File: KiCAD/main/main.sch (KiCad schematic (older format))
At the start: 2 parts

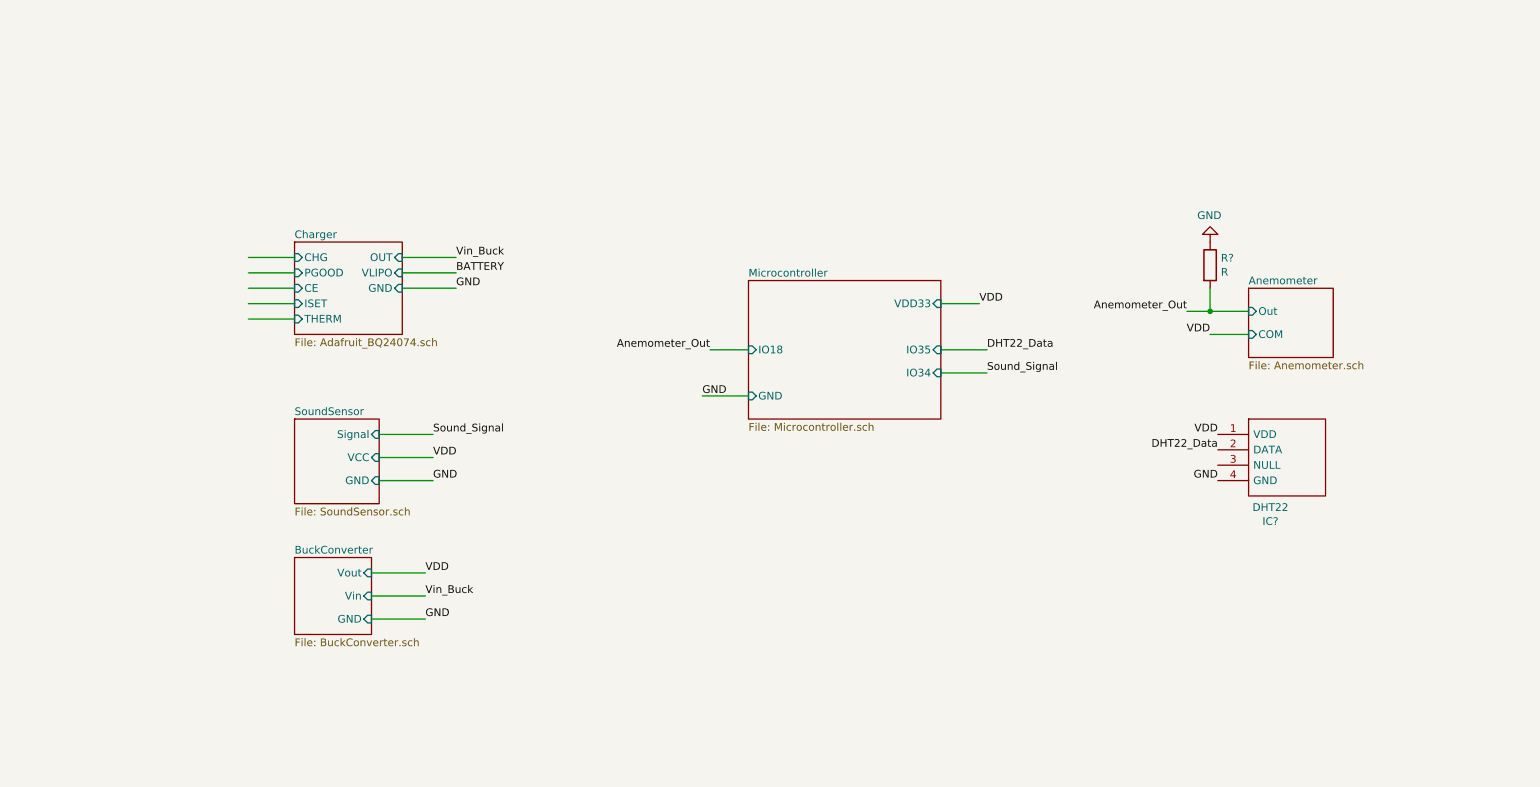
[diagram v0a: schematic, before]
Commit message: Improve readability on main schematic
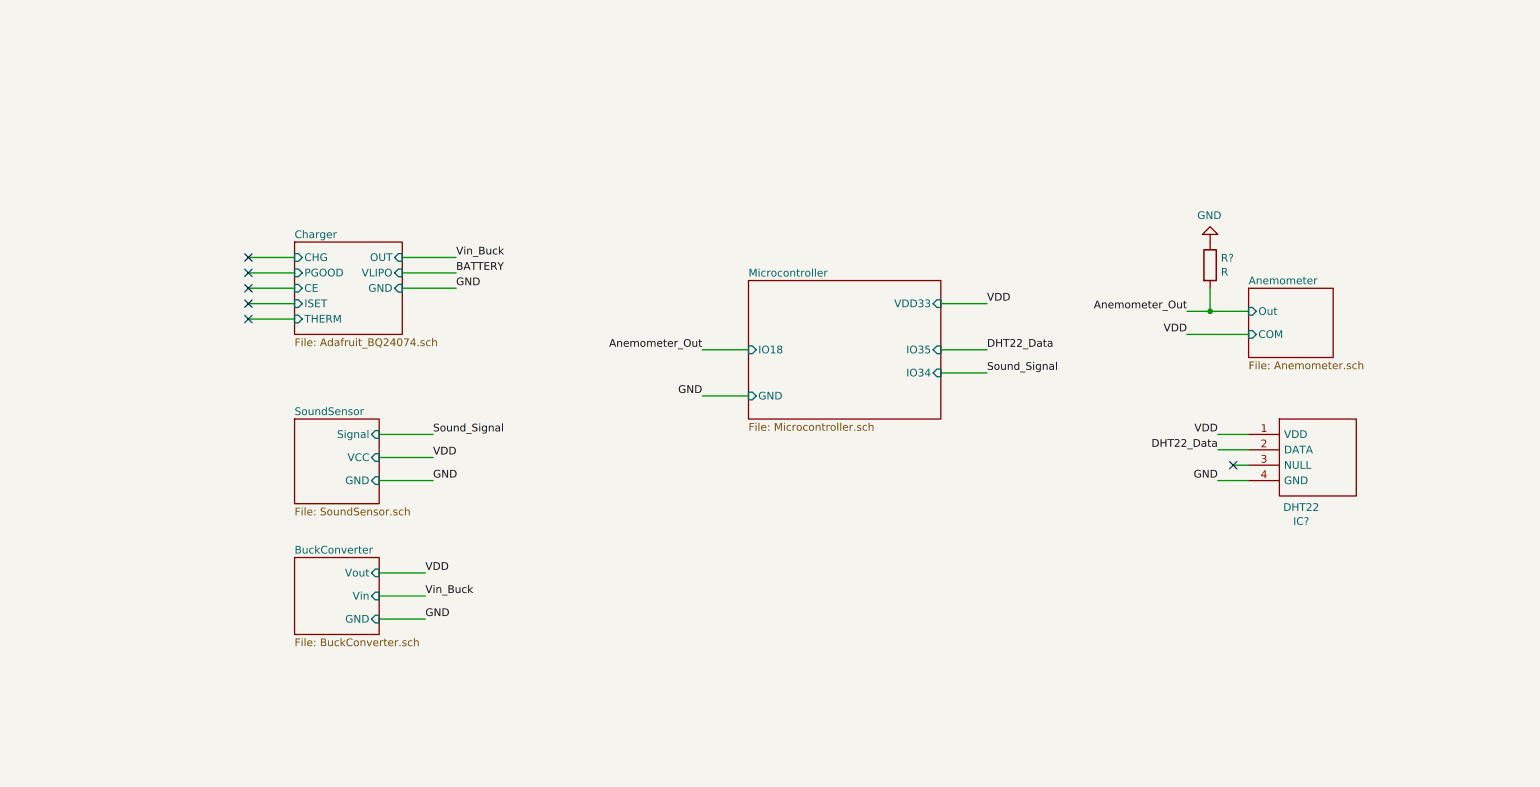
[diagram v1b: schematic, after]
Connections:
- wire segments 23 -> 27
- no-connect marks 0 -> 6
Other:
- moved on the sheet: IC?
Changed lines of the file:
@@
 $EndDescr
 $Sheet
-S 2450 3450 550  550
-U 5FAFBD3D
-F0 "SoundSensor" 50
-F1 "SoundSensor.sch" 50
-F2 "GND" I R 3000 3850 50
-F3 "VCC" I R 3000 3700 50
-F4 "Signal" I R 3000 3550 50
-$EndSheet
-$Sheet
-S 2450 4350 500  500
+S 2450 4350 550  500
 U 5FB0CF58
 F0 "BuckConverter" 50
 F1 "BuckConverter.sch" 50
-F2 "Vin" I R 2950 4600 50
-F3 "Vout" I R 2950 4450 50
-F4 "GND" I R 2950 4750 50
+F2 "Vin" I R 3000 4600 50
+F3 "Vout" I R 3000 4450 50
+F4 "GND" I R 3000 4750 50
 $EndSheet
-Wire Wire Line
-	6650 2700 6900 2700
 Wire Wire Line
 	3000 3700 3350 3700
 Text Label 3350 3700 0    50   ~ 0
 VDD
-Text Label 6900 2700 0    50   ~ 0
+Text Label 6950 2700 0    50   ~ 0
 VDD
-Wire Wire Line
-	2950 4450 3300 4450
 Text Label 3300 4450 0    50   ~ 0
 VDD
-Wire Wire Line
-	2950 4600 3300 4600
 Text Label 3300 4600 0    50   ~ 0
 Vin_Buck
@@
 	3000 3850 3350 3850
 Wire Wire Line
-	2950 4750 3300 4750
-Wire Wire Line
 	5400 3300 5100 3300
-Text Label 5100 3300 0    50   ~ 0
+Text Label 5100 3300 2    50   ~ 0
 GND
 Text Label 3300 4750 0    50   ~ 0
@@
 L DHT22:DHT22 IC?
 U 1 1 5FB3BE3A
-P 8450 3550
-F 0 "IC?" H 8792 2985 50  0000 C CNN
-F 1 "DHT22" H 8792 3076 50  0000 C CNN
-F 2 "DHT22" H 9200 3650 50  0001 L CNN
-F 3 "https://datasheet4u.com/datasheet-parts/DHT22-datasheet.php?id=792211" H 9200 3550 50  0001 L CNN
-F 4 "Digital-output relative humidity & temperature sensor/module DHT22" H 9200 3450 50  0001 L CNN "Description"
-F 5 "25.1" H 9200 3350 50  0001 L CNN "Height"
-F 6 "Aosong Electronics" H 9200 3250 50  0001 L CNN "Manufacturer_Name"
-F 7 "DHT22" H 9200 3150 50  0001 L CNN "Manufacturer_Part_Number"
-F 8 "" H 9200 3050 50  0001 L CNN "Arrow Part Number"
-F 9 "" H 9200 2950 50  0001 L CNN "Arrow Price/Stock"
-F 10 "" H 9200 2850 50  0001 L CNN "Mouser Part Number"
-F 11 "" H 9200 2750 50  0001 L CNN "Mouser Price/Stock"
-	1    8450 3550
+P 8650 3550
+F 0 "IC?" H 8992 2985 50  0000 C CNN
+F 1 "DHT22" H 8992 3076 50  0000 C CNN
+F 2 "DHT22" H 9400 3650 50  0001 L CNN
+F 3 "https://datasheet4u.com/datasheet-parts/DHT22-datasheet.php?id=792211" H 9400 3550 50  0001 L CNN
+F 4 "Digital-output relative humidity & temperature sensor/module DHT22" H 9400 3450 50  0001 L CNN "Description"
+F 5 "25.1" H 9400 3350 50  0001 L CNN "Height"
+F 6 "Aosong Electronics" H 9400 3250 50  0001 L CNN "Manufacturer_Name"
+F 7 "DHT22" H 9400 3150 50  0001 L CNN "Manufacturer_Part_Number"
+F 8 "" H 9400 3050 50  0001 L CNN "Arrow Part Number"
+F 9 "" H 9400 2950 50  0001 L CNN "Arrow Price/Stock"
+F 10 "" H 9400 2850 50  0001 L CNN "Mouser Part Number"
+F 11 "" H 9400 2750 50  0001 L CNN "Mouser Price/Stock"
+	1    8650 3550
 	1    0    0    -1
 $EndComp
@@
 Wire Wire Line
 	8650 2750 8400 2750
-Wire Wire Line
-	8650 2900 8400 2900
 Wire Wire Line
 	8400 2750 8400 2600
@@
 	8400 2750 8250 2750
 Connection ~ 8400 2750
-Text Label 8400 2900 2    50   ~ 0
+Text Label 8250 2900 2    50   ~ 0
 VDD
 Text Label 8250 2750 2    50   ~ 0
 Anemometer_Out
-Wire Wire Line
-	5400 3000 5150 3000
-Text Label 5150 3000 2    50   ~ 0
+Text Label 5100 3000 2    50   ~ 0
 Anemometer_Out
 $Sheet
@@
 F0 "Microcontroller" 50
 F1 "Microcontroller.sch" 50
-F14 "IO18" I L 5400 3000 50
-F24 "IO34" I R 6650 3150 50
-F25 "IO35" I R 6650 3000 50
-F35 "VDD33" I R 6650 2700 50
-F36 "GND" I L 5400 3300 50
+F2 "IO18" I L 5400 3000 50
+F3 "IO34" I R 6650 3150 50
+F4 "IO35" I R 6650 3000 50
+F5 "VDD33" I R 6650 2700 50
+F6 "GND" I L 5400 3300 50
 $EndSheet
+NoConn ~ 2150 2400
+NoConn ~ 2150 2500
+NoConn ~ 2150 2600
+NoConn ~ 2150 2700
+NoConn ~ 2150 2800
+Wire Wire Line
+	5100 3000 5400 3000
+Wire Wire Line
+	6950 2700 6650 2700
+Wire Wire Line
+	8250 2900 8650 2900
+Wire Wire Line
+	8450 3550 8650 3550
+Wire Wire Line
+	8650 3650 8450 3650
+Wire Wire Line
+	8650 3850 8450 3850
+NoConn ~ 8550 3750
+Wire Wire Line
+	8650 3750 8550 3750
+$Sheet
+S 2450 3450 550  550
+U 5FAFBD3D
+F0 "SoundSensor" 50
+F1 "SoundSensor.sch" 50
+F2 "GND" I R 3000 3850 50
+F3 "VCC" I R 3000 3700 50
+F4 "Signal" I R 3000 3550 50
+$EndSheet
+Wire Wire Line
+	3000 4450 3300 4450
+Wire Wire Line
+	3300 4600 3000 4600
+Wire Wire Line
+	3000 4750 3300 4750
 $EndSCHEMATC

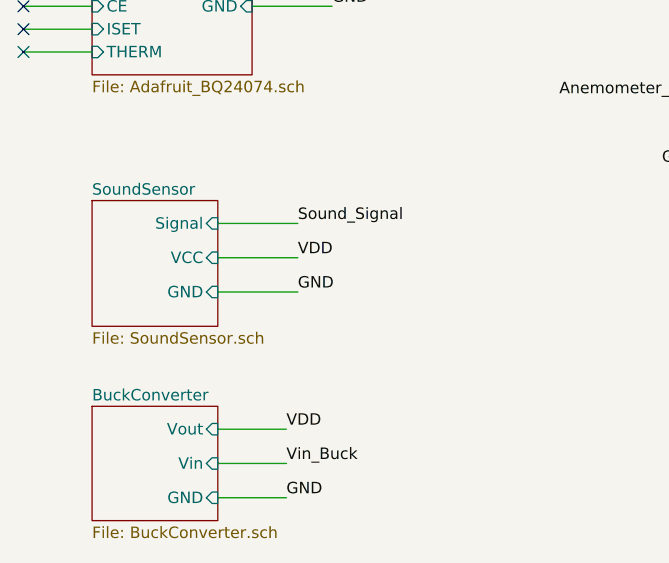
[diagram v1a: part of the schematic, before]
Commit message: Replace sound sensor and buck converter with the respective connectors
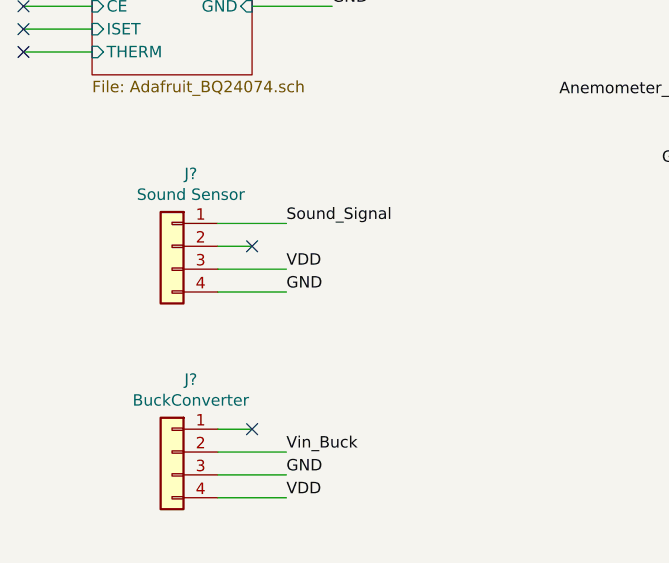
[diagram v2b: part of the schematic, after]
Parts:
- added J?: BuckConverter, Connector_PinSocket_2.54mm:PinSocket_1x04_P2.54mm_Vertical, symbol Connector_Generic:Conn_01x04
- added J?: Sound Sensor, Connector_JST:JST_PH_B4B-PH-K_1x04_P2.00mm_Vertical, symbol Connector_Generic:Conn_01x04
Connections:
- net GND: now also J?.3 (Pin_3), J?.4 (Pin_4)
- net Sound_Signal: now also J?.1 (Pin_1)
- net VDD: now also J?.3 (Pin_3), J?.4 (Pin_4)
- net Vin_Buck: now also J?.2 (Pin_2)
- no-connect marks 6 -> 8
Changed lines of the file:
@@
 $Descr A4 11693 8268
 encoding utf-8
-Sheet 1 6
+Sheet 1 4
 Title ""
 Date ""
@@
 Comment4 ""
 $EndDescr
-$Sheet
-S 2450 4350 550  500
-U 5FB0CF58
-F0 "BuckConverter" 50
-F1 "BuckConverter.sch" 50
-F2 "Vin" I R 3000 4600 50
-F3 "Vout" I R 3000 4450 50
-F4 "GND" I R 3000 4750 50
-$EndSheet
-Wire Wire Line
-	3000 3700 3350 3700
-Text Label 3350 3700 0    50   ~ 0
+Text Label 3300 3750 0    50   ~ 0
 VDD
 Text Label 6950 2700 0    50   ~ 0
 VDD
-Text Label 3300 4450 0    50   ~ 0
-VDD
-Text Label 3300 4600 0    50   ~ 0
+Text Label 3300 4750 0    50   ~ 0
+VDD
+Text Label 3300 4550 0    50   ~ 0
 Vin_Buck
-Wire Wire Line
-	3000 3850 3350 3850
 Wire Wire Line
 	5400 3300 5100 3300
 Text Label 5100 3300 2    50   ~ 0
 GND
-Text Label 3300 4750 0    50   ~ 0
-GND
-Text Label 3350 3850 0    50   ~ 0
-GND
-Wire Wire Line
-	3000 3550 3350 3550
-Text Label 3350 3550 0    50   ~ 0
+Text Label 3300 4650 0    50   ~ 0
+GND
+Text Label 3300 3850 0    50   ~ 0
+GND
+Text Label 3300 3550 0    50   ~ 0
 Sound_Signal
 Wire Wire Line
@@
 Wire Wire Line
 	8650 3750 8550 3750
-$Sheet
-S 2450 3450 550  550
-U 5FAFBD3D
-F0 "SoundSensor" 50
-F1 "SoundSensor.sch" 50
-F2 "GND" I R 3000 3850 50
-F3 "VCC" I R 3000 3700 50
-F4 "Signal" I R 3000 3550 50
-$EndSheet
-Wire Wire Line
-	3000 4450 3300 4450
-Wire Wire Line
-	3300 4600 3000 4600
 Wire Wire Line
 	3000 4750 3300 4750
+$Comp
+L Connector_Generic:Conn_01x04 J?
+U 1 1 5FC4DC93
+P 2800 4550
+F 0 "J?" H 2718 4867 50  0000 C CNN
+F 1 "BuckConverter" H 2718 4776 50  0000 C CNN
+F 2 "Connector_PinSocket_2.54mm:PinSocket_1x04_P2.54mm_Vertical" H 2800 4550 50  0001 C CNN
+F 3 "~" H 2800 4550 50  0001 C CNN
+	1    2800 4550
+	-1   0    0    -1
+$EndComp
+Wire Wire Line
+	3300 4550 3000 4550
+Wire Wire Line
+	3300 4650 3000 4650
+Wire Wire Line
+	3000 4450 3150 4450
+NoConn ~ 3150 4450
+$Comp
+L Connector_Generic:Conn_01x04 J?
+U 1 1 5FC5154E
+P 2800 3650
+F 0 "J?" H 2718 3967 50  0000 C CNN
+F 1 "Sound Sensor" H 2718 3876 50  0000 C CNN
+F 2 "Connector_JST:JST_PH_B4B-PH-K_1x04_P2.00mm_Vertical" H 2800 3650 50  0001 C CNN
+F 3 "~" H 2800 3650 50  0001 C CNN
+	1    2800 3650
+	-1   0    0    -1
+$EndComp
+NoConn ~ 3150 3650
+Wire Wire Line
+	3300 3850 3000 3850
+Wire Wire Line
+	3000 3750 3300 3750
+Wire Wire Line
+	3150 3650 3000 3650
+Wire Wire Line
+	3000 3550 3300 3550
 $EndSCHEMATC

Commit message: Add simple pcb design
still buggy
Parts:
- added J1: Charge Controller, Connector_JST:JST_PH_B2B-PH-K_1x02_P2.00mm_Vertical, symbol Connector_Generic:Conn_01x02
- added J4: Anemometer, Connector_JST:JST_PH_B2B-PH-K_1x02_P2.00mm_Vertical, symbol Connector_Generic:Conn_01x02
- R1: renamed from R?; footprint (none) -> Resistor_SMD:R_1206_3216Metric
- gave numbers to parts that had none: 3
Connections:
- net Anemometer_Out: now also J4.1 (Pin_1)
- net GND: now also J1.2 (Pin_2)
- net VDD: now also J4.2 (Pin_2)
- net Vin_Buck: now also J1.1 (Pin_1)
- no-connect marks 8 -> 3
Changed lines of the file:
@@
 $Descr A4 11693 8268
 encoding utf-8
-Sheet 1 4
+Sheet 1 2
 Title ""
 Date ""
@@
 Sound_Signal
 $Comp
-L DHT22:DHT22 IC?
+L DHT22:DHT22 IC1
 U 1 1 5FB3BE3A
 P 8650 3550
-F 0 "IC?" H 8992 2985 50  0000 C CNN
+F 0 "IC1" H 8992 2985 50  0000 C CNN
 F 1 "DHT22" H 8992 3076 50  0000 C CNN
 F 2 "DHT22" H 9400 3650 50  0001 L CNN
@@
 Text Label 8450 3650 2    50   ~ 0
 DHT22_Data
-$Sheet
-S 8650 2600 550  450
-U 5FB3DFB3
-F0 "Anemometer" 50
-F1 "Anemometer.sch" 50
-F2 "Out" I L 8650 2750 50
-F3 "COM" I L 8650 2900 50
-$EndSheet
 Wire Wire Line
 	8650 2750 8400 2750
@@
 	8400 2750 8400 2600
 $Comp
-L Device:R R?
+L Device:R R1
 U 1 1 5FB40072
 P 8400 2450
-F 0 "R?" H 8470 2496 50  0000 L CNN
+F 0 "R1" H 8470 2496 50  0000 L CNN
 F 1 "R" H 8470 2405 50  0000 L CNN
-F 2 "" V 8330 2450 50  0001 C CNN
+F 2 "Resistor_SMD:R_1206_3216Metric" V 8330 2450 50  0001 C CNN
 F 3 "~" H 8400 2450 50  0001 C CNN
 	1    8400 2450
@@
 $EndComp
 $Comp
-L power:GND #PWR?
+L power:GND #PWR01
 U 1 1 5FB404F7
 P 8400 2300
-F 0 "#PWR?" H 8400 2050 50  0001 C CNN
+F 0 "#PWR01" H 8400 2050 50  0001 C CNN
 F 1 "GND" H 8405 2127 50  0000 C CNN
 F 2 "" H 8400 2300 50  0001 C CNN
@@
 	8400 2750 8250 2750
 Connection ~ 8400 2750
-Text Label 8250 2900 2    50   ~ 0
+Text Label 8250 2850 2    50   ~ 0
 VDD
 Text Label 8250 2750 2    50   ~ 0
@@
 Text Label 5100 3000 2    50   ~ 0
 Anemometer_Out
-$Sheet
-S 2450 2300 700  600
-U 5FB60B8D
-F0 "Charger" 50
-F1 "Adafruit_BQ24074.sch" 50
-F2 "THERM" I L 2450 2800 50
-F3 "ISET" I L 2450 2700 50
-F4 "CE" I L 2450 2600 50
-F5 "PGOOD" I L 2450 2500 50
-F6 "CHG" I L 2450 2400 50
-F7 "OUT" I R 3150 2400 50
-F8 "VLIPO" I R 3150 2500 50
-F9 "GND" I R 3150 2600 50
-$EndSheet
-Wire Wire Line
-	3150 2400 3500 2400
-Wire Wire Line
-	3150 2500 3500 2500
-Wire Wire Line
-	3150 2600 3500 2600
-Wire Wire Line
-	2450 2400 2150 2400
-Wire Wire Line
-	2450 2500 2150 2500
-Wire Wire Line
-	2450 2600 2150 2600
-Wire Wire Line
-	2450 2700 2150 2700
-Wire Wire Line
-	2450 2800 2150 2800
-Text Label 3500 2400 0    50   ~ 0
+Text Label 3300 2500 0    50   ~ 0
 Vin_Buck
-Text Label 3500 2600 0    50   ~ 0
+Text Label 3300 2600 0    50   ~ 0
 GND
-Text Label 3500 2500 0    50   ~ 0
-BATTERY
 $Sheet
 S 5400 2550 1250 900
@@
 F6 "GND" I L 5400 3300 50
 $EndSheet
-NoConn ~ 2150 2400
-NoConn ~ 2150 2500
-NoConn ~ 2150 2600
-NoConn ~ 2150 2700
-NoConn ~ 2150 2800
 Wire Wire Line
 	5100 3000 5400 3000
@@
 	6950 2700 6650 2700
 Wire Wire Line
-	8250 2900 8650 2900
+	8250 2850 8650 2850
 Wire Wire Line
 	8450 3550 8650 3550
@@
 	3000 4750 3300 4750
 $Comp
-L Connector_Generic:Conn_01x04 J?
+L Connector_Generic:Conn_01x04 J3
 U 1 1 5FC4DC93
 P 2800 4550
-F 0 "J?" H 2718 4867 50  0000 C CNN
+F 0 "J3" H 2718 4867 50  0000 C CNN
 F 1 "BuckConverter" H 2718 4776 50  0000 C CNN
 F 2 "Connector_PinSocket_2.54mm:PinSocket_1x04_P2.54mm_Vertical" H 2800 4550 50  0001 C CNN
@@
 NoConn ~ 3150 4450
 $Comp
-L Connector_Generic:Conn_01x04 J?
+L Connector_Generic:Conn_01x04 J2
 U 1 1 5FC5154E
 P 2800 3650
-F 0 "J?" H 2718 3967 50  0000 C CNN
+F 0 "J2" H 2718 3967 50  0000 C CNN
 F 1 "Sound Sensor" H 2718 3876 50  0000 C CNN
 F 2 "Connector_JST:JST_PH_B4B-PH-K_1x04_P2.00mm_Vertical" H 2800 3650 50  0001 C CNN
@@
 Wire Wire Line
 	3000 3550 3300 3550
+$Comp
+L Connector_Generic:Conn_01x02 J1
+U 1 1 5FC604E2
+P 2800 2500
+F 0 "J1" H 2718 2717 50  0000 C CNN
+F 1 "Charge Controller" H 2718 2626 50  0000 C CNN
+F 2 "Connector_JST:JST_PH_B2B-PH-K_1x02_P2.00mm_Vertical" H 2800 2500 50  0001 C CNN
+F 3 "~" H 2800 2500 50  0001 C CNN
+	1    2800 2500
+	-1   0    0    -1
+$EndComp
+Wire Wire Line
+	3300 2500 3000 2500
+Wire Wire Line
+	3300 2600 3000 2600
+$Comp
+L Connector_Generic:Conn_01x02 J4
+U 1 1 5FC61584
+P 8850 2750
+F 0 "J4" H 8930 2742 50  0000 L CNN
+F 1 "Anemometer" H 8930 2651 50  0000 L CNN
+F 2 "Connector_JST:JST_PH_B2B-PH-K_1x02_P2.00mm_Vertical" H 8850 2750 50  0001 C CNN
+F 3 "~" H 8850 2750 50  0001 C CNN
+	1    8850 2750
+	1    0    0    -1
+$EndComp
 $EndSCHEMATC

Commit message: alimentação e proteção
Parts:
- added Q? (x2): Q_NPN_BCE, symbol Device:Q_NPN_BCE
- added R2: R, symbol Device:R
- added R3, R? (x4): R, Resistor_SMD:R_1206_3216Metric, symbol Device:R
- added U1: 4N25, Package_DIP:DIP-6_W7.62mm, symbol Isolator:4N25
- added U?: 4020, symbol 4xxx:4020
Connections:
- net Anemometer_Out: now also U?.10 (CLK)
- net DHT22_Data: now also R2.1
- net GND: now also R3.2, R?.2, R?.2, U1.2, U?.8 (VSS)
- net VDD: now also Q?.2 (C), Q?.2 (C), U1.5, U?.16 (VDD); no longer IC1.1 (VDD), J2.3 (Pin_3)
- new net: IC1.1 (VDD), Q?.3 (E), R?.1
- new net: J2.3 (Pin_3), Q?.3 (E), R?.1
- new net: R2.2, U1.1
- new net: Q?.1 (B), R?.2 (x2)
- new net Microcontroller/I021: U?.6 (Q6)
- new net Microcontroller/IO16: U?.9 (Q0)
- new net Microcontroller/IO17: U?.7 (Q3)
- new net Microcontroller/IO18: U?.5 (Q4)
- new net Microcontroller/IO19: U?.4 (Q5)
- new net Microcontroller/IO22: U?.13 (Q7)
- new net Microcontroller/IO23: U?.12 (Q8)
- new net Microcontroller/IO25: U?.14 (Q9)
- new net Microcontroller/IO26: U?.15 (Q10)
- new net Microcontroller/IO27: U?.1 (Q11)
- new net Microcontroller/IO32: U?.2 (Q12)
- new net Microcontroller/IO33: U?.3 (Q13)
- new net Opto_DHT22_Data: R3.1, U1.4
- new net reset_counter: U?.11 (Reset)
- new net supply_on: R?.1, R?.1
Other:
- moved on the sheet: IC1, J1, J2, J3, J4, R1

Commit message: algumas correções
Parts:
- removed J1: Charge Controller, Connector_JST:JST_PH_B2B-PH-K_1x02_P2.00mm_Vertical, symbol Connector_Generic:Conn_01x02
- removed Q? (x2): Q_NPN_BCE, symbol Device:Q_NPN_BCE
- removed R? (x2): R, Resistor_SMD:R_1206_3216Metric, symbol Device:R
- added J1: Charge controller, symbol Connector_Generic:Conn_01x03
- added Q1: Q_NJFET_DGS, symbol Device:Q_NJFET_DGS
- added U2: 4N25, Package_DIP:DIP-6_W7.62mm, symbol Isolator:4N25
- R1: value R -> 1k; footprint Resistor_SMD:R_1206_3216Metric -> (none)
- R2: value R -> 1k
- R3: value R -> 10k
- gave numbers to parts that had none: 1
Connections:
- net Anemometer_Out: now also R2.1; no longer R1.2, U1.10 (CLK)
- net DHT22_Data: no longer R2.1
- net GND: now also J1.2 (Pin_2), U2.2; no longer R1.1
- net VDD: now also Q1.1 (D), U2.5
- net Vin_Buck: now also J1.1 (Pin_1)
- net supply_on: now also R1.1
- net VDD_on: now reaches IC1.1 (VDD)
- net VDD_on: now also J2.3 (Pin_3), R?.1, Q1.3 (S), U2.4
- net at R?.2: now also Q1.2 (G)
- net Opto_DHT22_Data renamed Opto_Anemometer_Out
- net Opto_Anemometer_Out: now also U1.10 (CLK)
- new net: R1.2, U2.1
- new net Battery_status: J1.3 (Pin_3)
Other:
- moved on the sheet: J4, R2, R3, R?, U1
